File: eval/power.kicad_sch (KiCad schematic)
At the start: 40 parts, among them Q1 BSC0702LS, Q2 BSC0702LS, U2 LM5148RGYR, U3 INA180A3, U8 INA180A3

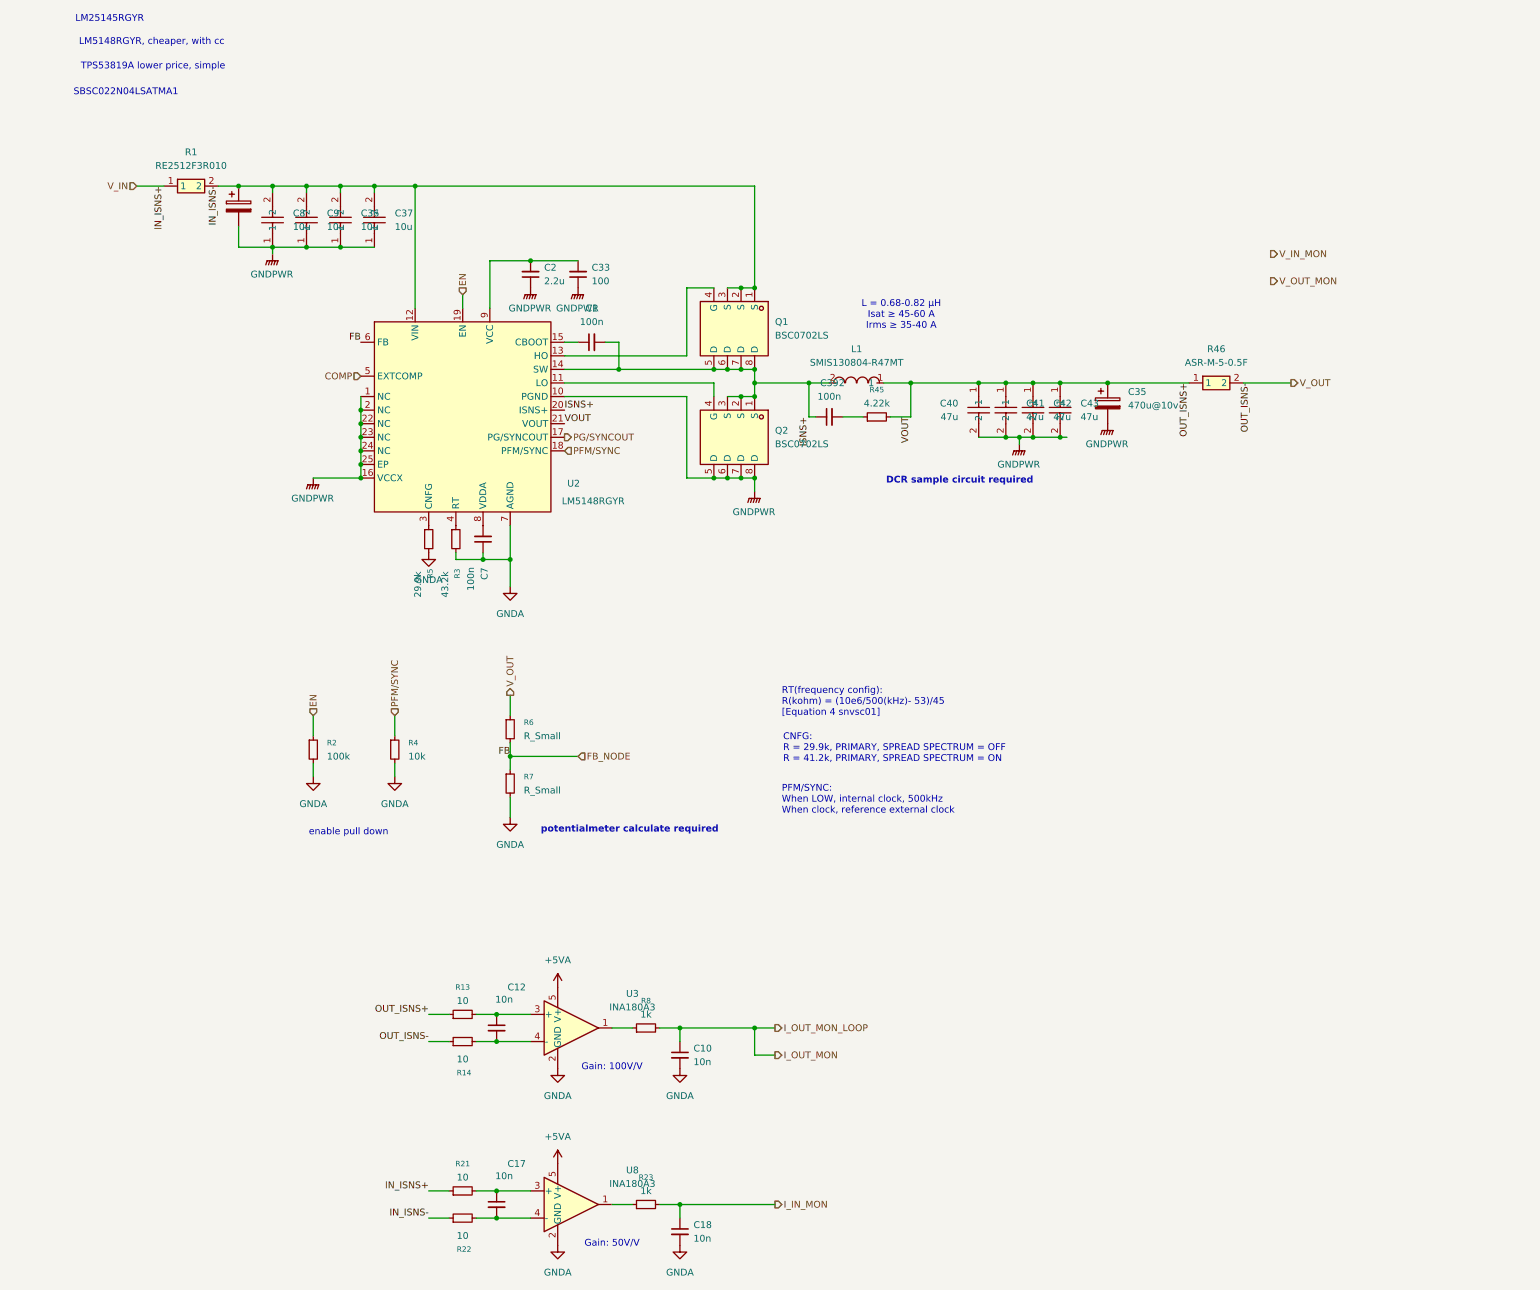
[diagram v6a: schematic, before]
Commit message: [sch] Add ORing for 2 input
plan to add back to back mos protection for output (high side mos)
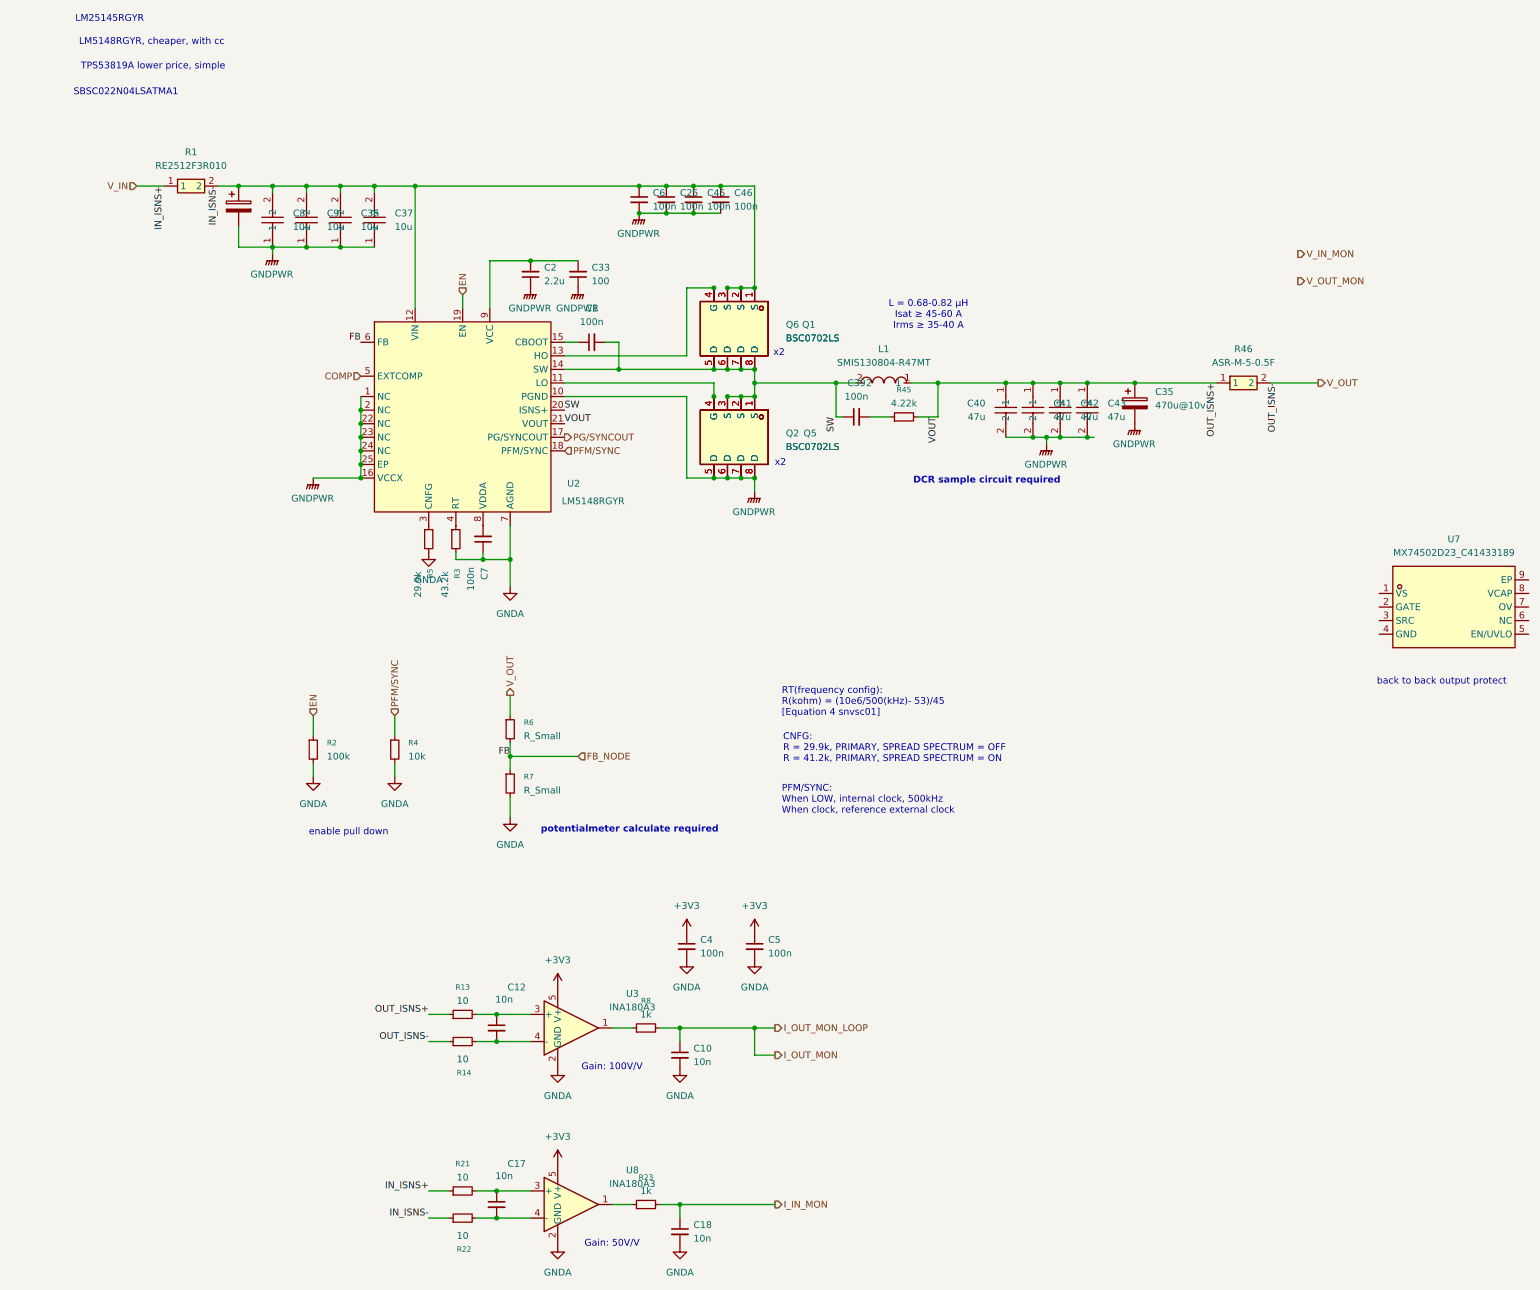
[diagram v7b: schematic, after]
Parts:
- added C25, C4, C45, C46, C5, C6: 100n, Capacitor_SMD:C_0603_1608Metric, symbol Device:C_Small
- added Q5, Q6: BSC0702LS, EasyEDA:PG-TDSON-8_L5.0-W6.0-P1.27-BL-EP, symbol EasyEDA:BSC0702LS
- added U7: MX74502D23_C41433189, EasyEDA:UDFN-8L_L2.0-W3.0-P0.50-BL-EP, symbol EasyEDA:MX74502D23_C41433189
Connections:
- net GNDA: now also C4.2, C5.2
- net GNDPWR: now also C25.2, C45.2, C46.2, C6.2, Q5.5 (D), Q5.6 (D), Q5.7 (D), Q5.8 (D)
- net IN_ISNS-: now also C25.1, C45.1, C46.1, C6.1, Q6.1 (S), Q6.2 (S), Q6.3 (S)
- net at Q2.4 (G), U2.11 (LO): now also Q5.4 (G)
- net at Q1.4 (G), U2.13 (HO): now also Q6.4 (G)
- net +5VA renamed +3V3
- net +3V3: now also C4.1, C5.1
- net ISNS+ renamed SW
- net SW: now also Q5.1 (S), Q5.2 (S), Q5.3 (S), Q6.5 (D), Q6.6 (D), Q6.7 (D), Q6.8 (D)
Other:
- note added: "back to back output protect"
- note added: "x2"
- moved on the sheet: C35, C39, C40, C41, C42, C43, L1, R45, R46

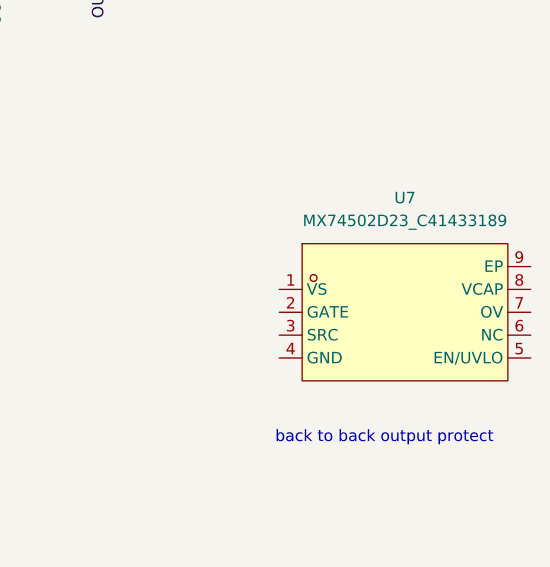
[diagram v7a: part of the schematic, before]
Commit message: [sch] add back to back protection (MX74502)
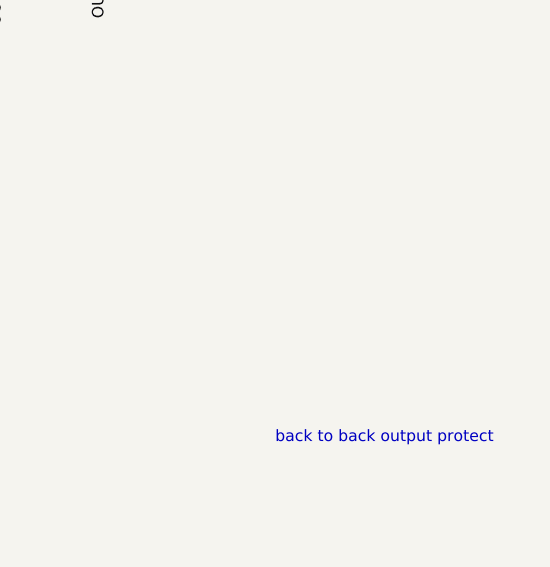
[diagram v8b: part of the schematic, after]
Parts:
- removed U7: MX74502D23_C41433189, EasyEDA:UDFN-8L_L2.0-W3.0-P0.50-BL-EP, symbol EasyEDA:MX74502D23_C41433189
